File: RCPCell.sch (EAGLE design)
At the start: 22 parts, among them IC1 SIM900, Q1 BSS84, Q2 BSS84, U1 PESDXS4UD

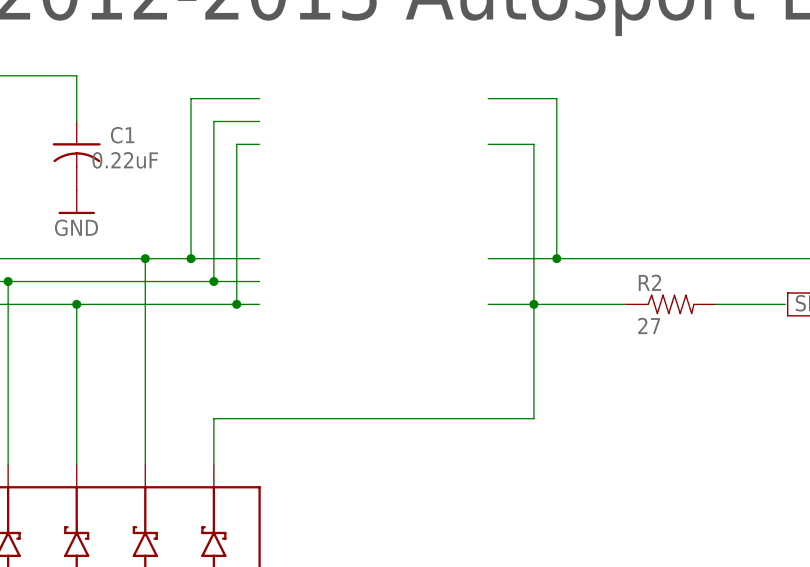
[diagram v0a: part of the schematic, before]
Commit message: placeholder simcard
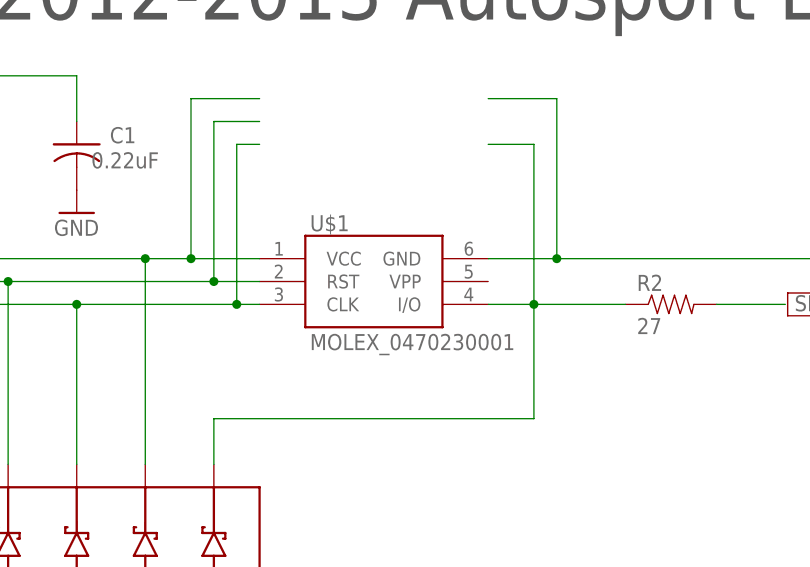
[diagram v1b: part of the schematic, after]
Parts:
- added U$1: MOLEX_0470230001, simcard:MOLEX_0470230001
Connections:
- net GND: now also U$1.GND
- net SIM_CLK_CARD: now also U$1.CLK
- net SIM_DATA_CARD: now also U$1.I/O
- net SIM_RST_CARD: now also U$1.RST
- net SIM_VDD: now also U$1.VCC
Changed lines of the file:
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@@
 <part name="AD156" library="supply2" deviceset="V--&gt;" device="" value=""/>
 <part name="J$1" library="SparkFun" deviceset="SMA_EDGE" device=""/>
+<part name="U$1" library="simcard" deviceset="MOLEX_0470230001" device=""/>
 </parts>
 <sheets>
@@
 </instance>
 <instance part="J$1" gate="1" x="-10.16" y="149.86"/>
+<instance part="U$1" gate="G$1" x="137.16" y="142.24"/>
 </instances>
 <busses>
@@
 <junction x="157.48" y="144.78"/>
 <pinref part="GND7" gate="1" pin="GND"/>
+<pinref part="U$1" gate="G$1" pin="GND"/>
 </segment>
 <segment>
@@
 <pinref part="C1" gate="G$1" pin="1"/>
 <pinref part="U1" gate="G$1" pin="4"/>
+<pinref part="U$1" gate="G$1" pin="VCC"/>
 </segment>
 </net>
@@
 <pinref part="R2" gate="G$1" pin="1"/>
 <pinref part="U1" gate="G$1" pin="6"/>
+<pinref part="U$1" gate="G$1" pin="I/O"/>
 </segment>
 </net>
@@
 <pinref part="R1" gate="G$1" pin="2"/>
 <pinref part="U1" gate="G$1" pin="1"/>
+<pinref part="U$1" gate="G$1" pin="RST"/>
 </segment>
 </net>
@@
 <pinref part="R3" gate="G$1" pin="2"/>
 <pinref part="U1" gate="G$1" pin="3"/>
+<pinref part="U$1" gate="G$1" pin="CLK"/>
 </segment>
 </net>

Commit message: WIP for MK2 version of cell module
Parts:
- U$1: value MOLEX_0470230001 -> MOLEX_04702300012; device simcard:MOLEX_0470230001 -> simcard:MOLEX_04702300012
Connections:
- removed net N$2: NETLIGHT.A, R8.1
- new net N$1: NETLIGHT.C, R8.2
- net GND: now also R8.1; no longer NETLIGHT.C
- net STATUS: now also NETLIGHT.A; no longer R8.2
- net USB_DM_HS_OUT: now also EX1.3; no longer EX1.4
- net USB_DP_HS_OUT: now also EX1.4; no longer EX1.3
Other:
- note added: "Copyright 2012-2014 Autosport Labs"
- note removed: "Copyright 2012-2013 Autosport Labs"
- moved on the sheet: NETLIGHT
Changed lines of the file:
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@@
 <part name="AD156" library="supply2" deviceset="V--&gt;" device="" value=""/>
 <part name="J$1" library="SparkFun" deviceset="SMA_EDGE" device=""/>
-<part name="U$1" library="simcard" deviceset="MOLEX_0470230001" device=""/>
+<part name="U$1" library="simcard" deviceset="MOLEX_0470230001" device="2"/>
 </parts>
 <sheets>
@@
 <plain>
 <text x="109.22" y="-12.7" size="3.81" layer="97" ratio="5">RaceCapture P2P Telemetry</text>
-<text x="200.66" y="177.8" size="6.4516" layer="97" rot="R180">Copyright 2012-2013 Autosport Labs</text>
+<text x="200.66" y="177.8" size="6.4516" layer="97" rot="R180">Copyright 2012-2014 Autosport Labs</text>
 <text x="200.66" y="190.5" size="6.4516" layer="97" rot="R180">RaceCapture Cell Telemetry</text>
 <text x="113.03" y="201.803" size="6.4516" layer="97" font="vector">autosportlabs.com</text>
@@
 <instance part="R8" gate="G$1" x="-187.96" y="-2.54" rot="R90"/>
 <instance part="GND4" gate="1" x="-187.96" y="-22.86"/>
-<instance part="NETLIGHT" gate="G$1" x="-187.96" y="-13.716"/>
+<instance part="NETLIGHT" gate="G$1" x="-187.96" y="9.144"/>
 <instance part="GND62" gate="1" x="104.14" y="7.62"/>
 <instance part="P+16" gate="1" x="175.26" y="63.5"/>
@@
 <nets>
 <net name="GND" class="0">
-<segment>
-<wire x1="-187.96" y1="-17.78" x2="-187.96" y2="-20.32" width="0.1524" layer="91"/>
-<pinref part="GND4" gate="1" pin="GND"/>
-<pinref part="NETLIGHT" gate="G$1" pin="C"/>
-</segment>
 <segment>
 <wire x1="104.14" y1="10.16" x2="104.14" y2="12.7" width="0.1524" layer="91"/>
@@
 </segment>
 <segment>
-<wire x1="149.86" y1="144.78" x2="157.48" y2="144.78" width="0.1524" layer="91"/>
-<wire x1="157.48" y1="144.78" x2="203.2" y2="144.78" width="0.1524" layer="91"/>
+<wire x1="149.86" y1="144.78" x2="203.2" y2="144.78" width="0.1524" layer="91"/>
 <wire x1="203.2" y1="144.78" x2="203.2" y2="134.62" width="0.1524" layer="91"/>
-<wire x1="149.86" y1="162.56" x2="157.48" y2="162.56" width="0.1524" layer="91"/>
-<wire x1="157.48" y1="162.56" x2="157.48" y2="144.78" width="0.1524" layer="91"/>
-<junction x="157.48" y="144.78"/>
 <pinref part="GND7" gate="1" pin="GND"/>
 <pinref part="U$1" gate="G$1" pin="GND"/>
@@
 <junction x="-17.78" y="142.24"/>
 <junction x="-17.78" y="139.7"/>
+</segment>
+<segment>
+<pinref part="R8" gate="G$1" pin="1"/>
+<pinref part="GND4" gate="1" pin="GND"/>
+<wire x1="-187.96" y1="-20.32" x2="-187.96" y2="-7.62" width="0.1524" layer="91"/>
 </segment>
 </net>
@@
 </segment>
 </net>
-<net name="N$2" class="0">
-<segment>
-<wire x1="-187.96" y1="-7.62" x2="-187.96" y2="-10.16" width="0.1524" layer="91"/>
-<pinref part="R8" gate="G$1" pin="1"/>
-<pinref part="NETLIGHT" gate="G$1" pin="A"/>
-</segment>
-</net>
 <net name="+5V" class="0">
 <segment>
@@
 <segment>
 <wire x1="-198.12" y1="17.78" x2="-187.96" y2="17.78" width="0.1524" layer="91"/>
-<wire x1="-187.96" y1="2.54" x2="-187.96" y2="17.78" width="0.1524" layer="91"/>
 <label x="-199.39" y="18.542" size="1.778" layer="95" rot="R180"/>
-<pinref part="R8" gate="G$1" pin="2"/>
+<pinref part="NETLIGHT" gate="G$1" pin="A"/>
+<wire x1="-187.96" y1="17.78" x2="-187.96" y2="12.7" width="0.1524" layer="91"/>
 </segment>
 <segment>
@@
 </segment>
 <segment>
-<wire x1="124.46" y1="144.78" x2="116.84" y2="144.78" width="0.1524" layer="91"/>
-<wire x1="116.84" y1="144.78" x2="111.76" y2="144.78" width="0.1524" layer="91"/>
+<wire x1="124.46" y1="144.78" x2="111.76" y2="144.78" width="0.1524" layer="91"/>
 <wire x1="111.76" y1="144.78" x2="91.44" y2="144.78" width="0.1524" layer="91"/>
 <wire x1="91.44" y1="144.78" x2="91.44" y2="147.32" width="0.1524" layer="91"/>
@@
 <wire x1="104.14" y1="165.1" x2="78.74" y2="165.1" width="0.1524" layer="91"/>
 <wire x1="78.74" y1="165.1" x2="78.74" y2="147.32" width="0.1524" layer="91"/>
-<wire x1="124.46" y1="162.56" x2="116.84" y2="162.56" width="0.1524" layer="91"/>
-<wire x1="116.84" y1="162.56" x2="116.84" y2="144.78" width="0.1524" layer="91"/>
 <wire x1="111.76" y1="121.92" x2="111.76" y2="144.78" width="0.1524" layer="91"/>
 <junction x="78.74" y="147.32"/>
-<junction x="116.84" y="144.78"/>
 <junction x="111.76" y="144.78"/>
 <label x="70.358" y="148.336" size="1.778" layer="95" rot="R180"/>
@@
 <wire x1="154.94" y1="127" x2="119.38" y2="127" width="0.1524" layer="91"/>
 <wire x1="119.38" y1="127" x2="119.38" y2="121.92" width="0.1524" layer="91"/>
-<wire x1="149.86" y1="157.48" x2="154.94" y2="157.48" width="0.1524" layer="91"/>
-<wire x1="154.94" y1="157.48" x2="154.94" y2="139.7" width="0.1524" layer="91"/>
 <junction x="154.94" y="139.7"/>
 <pinref part="R2" gate="G$1" pin="1"/>
@@
 <net name="SIM_RST_CARD" class="0">
 <segment>
-<wire x1="124.46" y1="142.24" x2="119.38" y2="142.24" width="0.1524" layer="91"/>
-<wire x1="119.38" y1="142.24" x2="96.52" y2="142.24" width="0.1524" layer="91"/>
+<wire x1="124.46" y1="142.24" x2="96.52" y2="142.24" width="0.1524" layer="91"/>
 <wire x1="96.52" y1="142.24" x2="93.98" y2="142.24" width="0.1524" layer="91"/>
-<wire x1="124.46" y1="160.02" x2="119.38" y2="160.02" width="0.1524" layer="91"/>
-<wire x1="119.38" y1="160.02" x2="119.38" y2="142.24" width="0.1524" layer="91"/>
 <wire x1="96.52" y1="142.24" x2="96.52" y2="121.92" width="0.1524" layer="91"/>
-<junction x="119.38" y="142.24"/>
 <junction x="96.52" y="142.24"/>
 <pinref part="R1" gate="G$1" pin="2"/>
@@
 <net name="SIM_CLK_CARD" class="0">
 <segment>
-<wire x1="124.46" y1="139.7" x2="121.92" y2="139.7" width="0.1524" layer="91"/>
-<wire x1="121.92" y1="139.7" x2="104.14" y2="139.7" width="0.1524" layer="91"/>
+<wire x1="124.46" y1="139.7" x2="104.14" y2="139.7" width="0.1524" layer="91"/>
 <wire x1="104.14" y1="139.7" x2="91.44" y2="139.7" width="0.1524" layer="91"/>
 <wire x1="91.44" y1="139.7" x2="91.44" y2="137.16" width="0.1524" layer="91"/>
 <wire x1="91.44" y1="137.16" x2="86.36" y2="137.16" width="0.1524" layer="91"/>
-<wire x1="124.46" y1="157.48" x2="121.92" y2="157.48" width="0.1524" layer="91"/>
-<wire x1="121.92" y1="157.48" x2="121.92" y2="139.7" width="0.1524" layer="91"/>
 <wire x1="104.14" y1="121.92" x2="104.14" y2="139.7" width="0.1524" layer="91"/>
-<junction x="121.92" y="139.7"/>
 <junction x="104.14" y="139.7"/>
 <pinref part="R3" gate="G$1" pin="2"/>
@@
 </segment>
 </net>
-<net name="USB_DP_HS_OUT" class="0">
+<net name="USB_DM_HS_OUT" class="0">
 <segment>
 <pinref part="EX1" gate="1" pin="3"/>
@@
 </segment>
 </net>
-<net name="USB_DM_HS_OUT" class="0">
+<net name="USB_DP_HS_OUT" class="0">
 <segment>
 <pinref part="EX1" gate="1" pin="4"/>
@@
 </segment>
 </net>
+<net name="N$1" class="0">
+<segment>
+<pinref part="R8" gate="G$1" pin="2"/>
+<pinref part="NETLIGHT" gate="G$1" pin="C"/>
+<wire x1="-187.96" y1="5.08" x2="-187.96" y2="2.54" width="0.1524" layer="91"/>
+</segment>
+</net>

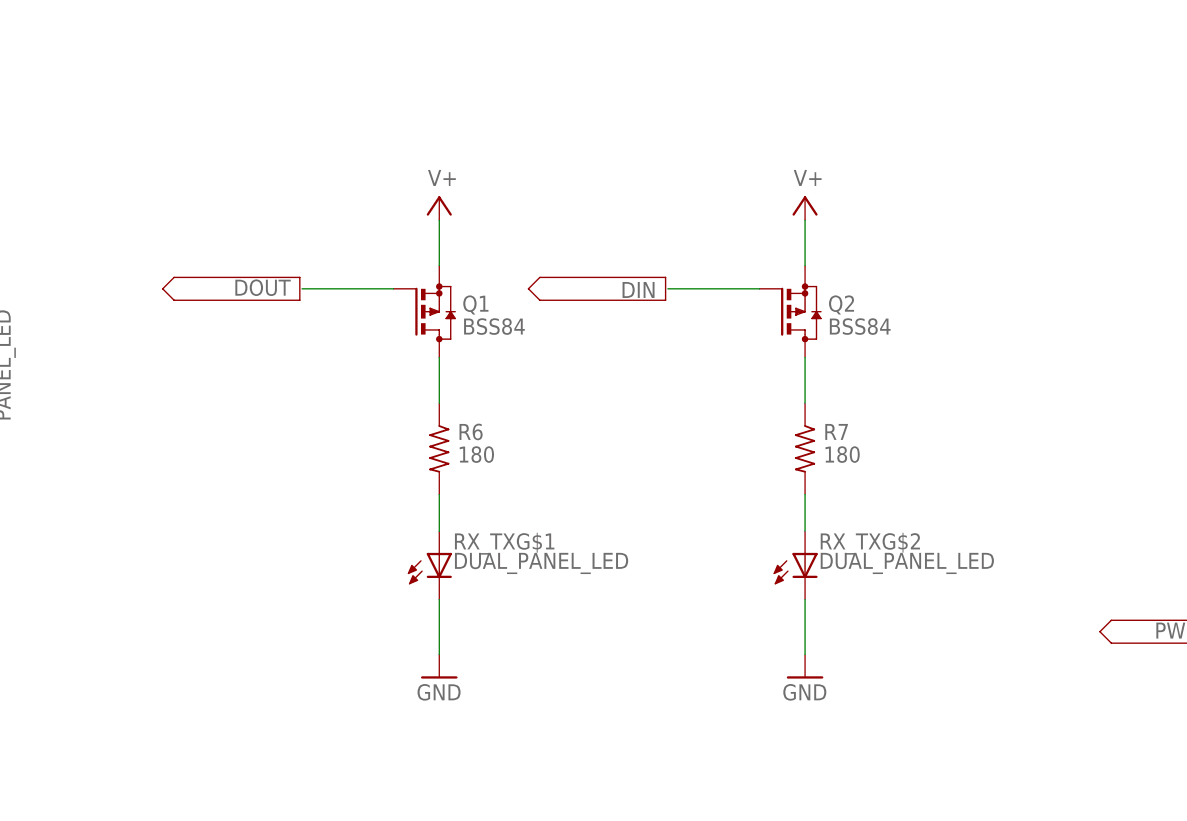
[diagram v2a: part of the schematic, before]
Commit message: WIP for cellular module, compacted board size
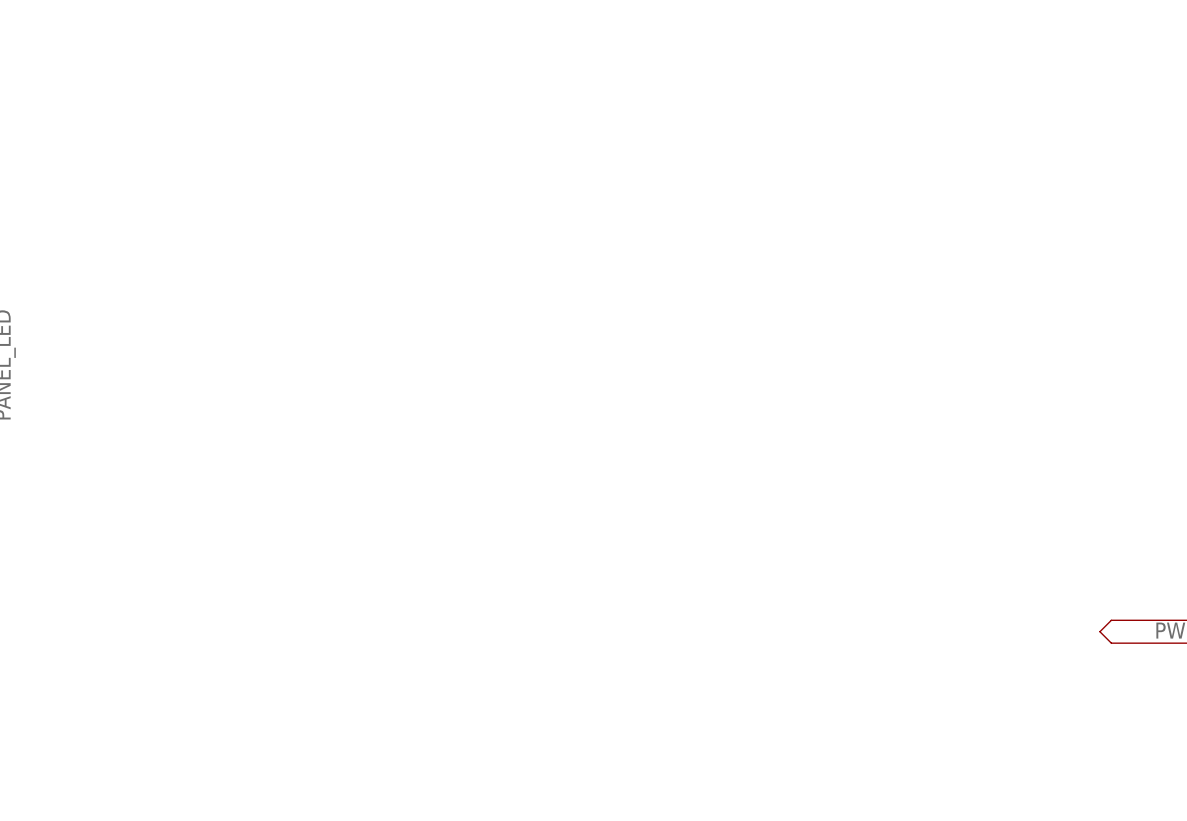
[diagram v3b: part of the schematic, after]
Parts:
- removed Q1, Q2: BSS84, transistor-small-signal:BSS84
- removed R6, R7: 180, rcl:R-US_R0603
- removed RX_TX: DUAL_PANEL_LED, LEDs:DUAL_PANEL_LED
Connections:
- removed net N$3: Q2.D, R7.1
- removed net N$4: R6.2, RX_TXG$1.A
- removed net N$5: Q1.D, R6.1
- removed net N$6: R7.2, RX_TXG$2.A
- net DIN: no longer Q2.G
- net DOUT: no longer Q1.G
- net GND: no longer RX_TXG$1.C, RX_TXG$2.C
- net V+: no longer Q1.S, Q2.S
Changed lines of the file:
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@@
 <part name="C1" library="rcl" deviceset="C-US" device="C0603" value="0.22uF"/>
 <part name="GND9" library="supply1" deviceset="GND" device=""/>
-<part name="R7" library="rcl" deviceset="R-US_" device="R0603" value="180"/>
-<part name="GND31" library="supply1" deviceset="GND" device=""/>
-<part name="RX_TX" library="LEDs" deviceset="DUAL_PANEL_LED" device=""/>
-<part name="P+5" library="supply2" deviceset="V+" device=""/>
-<part name="R6" library="rcl" deviceset="R-US_" device="R0603" value="180"/>
-<part name="GND3" library="supply1" deviceset="GND" device=""/>
-<part name="P+6" library="supply2" deviceset="V+" device=""/>
-<part name="Q1" library="transistor-small-signal" deviceset="BSS84" device=""/>
-<part name="Q2" library="transistor-small-signal" deviceset="BSS84" device=""/>
-<part name="AD9" library="supply2" deviceset="V--&gt;" device="" value=""/>
-<part name="AD11" library="supply2" deviceset="V--&gt;" device="" value=""/>
 <part name="AD10" library="supply2" deviceset="V--&gt;" device="" value=""/>
 <part name="U1" library="smt_diodes" deviceset="PESDXS4UD" device=""/>
@@
 </instance>
 <instance part="GND9" gate="1" x="104.14" y="149.86"/>
-<instance part="R7" gate="G$1" x="-93.98" y="2.54" smashed="yes" rot="R270">
-<attribute name="NAME" x="-91.948" y="3.5306" size="1.778" layer="95"/>
-<attribute name="VALUE" x="-91.948" y="1.016" size="1.778" layer="96"/>
-</instance>
-<instance part="GND31" gate="1" x="-93.98" y="-22.86"/>
-<instance part="RX_TX" gate="G$1" x="-134.62" y="-10.16" smashed="yes">
-<attribute name="NAME" x="-133.096" y="-8.636" size="1.778" layer="95"/>
-<attribute name="VALUE" x="-133.096" y="-10.795" size="1.778" layer="96"/>
-</instance>
-<instance part="RX_TX" gate="G$2" x="-93.98" y="-10.16" smashed="yes">
-<attribute name="NAME" x="-92.456" y="-8.636" size="1.778" layer="95"/>
-<attribute name="VALUE" x="-92.456" y="-10.795" size="1.778" layer="96"/>
-</instance>
-<instance part="P+5" gate="1" x="-93.98" y="30.48"/>
-<instance part="R6" gate="G$1" x="-134.62" y="2.54" smashed="yes" rot="R270">
-<attribute name="NAME" x="-132.588" y="3.5306" size="1.778" layer="95"/>
-<attribute name="VALUE" x="-132.588" y="1.016" size="1.778" layer="96"/>
-</instance>
-<instance part="GND3" gate="1" x="-134.62" y="-22.86"/>
-<instance part="P+6" gate="1" x="-134.62" y="30.48"/>
-<instance part="Q1" gate="G$1" x="-134.62" y="17.78"/>
-<instance part="Q2" gate="G$1" x="-93.98" y="17.78"/>
-<instance part="AD9" gate="G$1" x="-150.114" y="20.32" smashed="yes" rot="R180">
-<attribute name="VALUE" x="-151.384" y="21.082" size="1.778" layer="96" rot="R180"/>
-</instance>
-<instance part="AD11" gate="G$1" x="-109.474" y="20.32" smashed="yes" rot="R180">
-<attribute name="VALUE" x="-110.744" y="21.082" size="1.778" layer="96" rot="R180"/>
-</instance>
 <instance part="AD10" gate="G$1" x="33.02" y="142.494" smashed="yes" rot="R90">
 <attribute name="VALUE" x="33.782" y="143.764" size="1.778" layer="96" rot="R90"/>
@@
 </segment>
 <segment>
-<wire x1="-134.62" y1="-14.224" x2="-134.62" y2="-20.32" width="0.1524" layer="91"/>
-<pinref part="GND3" gate="1" pin="GND"/>
-<pinref part="RX_TX" gate="G$1" pin="C"/>
-</segment>
-<segment>
-<wire x1="-93.98" y1="-14.224" x2="-93.98" y2="-20.32" width="0.1524" layer="91"/>
-<pinref part="GND31" gate="1" pin="GND"/>
-<pinref part="RX_TX" gate="G$2" pin="C"/>
-</segment>
-<segment>
 <wire x1="111.76" y1="99.06" x2="111.76" y2="101.6" width="0.1524" layer="91"/>
 <pinref part="U1" gate="G$1" pin="2"/>
@@
 <pinref part="IC1" gate="G$1" pin="RXD"/>
 </segment>
-<segment>
-<wire x1="-99.06" y1="20.32" x2="-109.22" y2="20.32" width="0.1524" layer="91"/>
-<label x="-110.49" y="21.082" size="1.778" layer="95" rot="R180"/>
-<pinref part="Q2" gate="G$1" pin="G"/>
-</segment>
 </net>
 <net name="DOUT" class="0">
@@
 <label x="-41.402" y="92.202" size="1.778" layer="95" rot="R180"/>
 <pinref part="IC1" gate="G$1" pin="TXD"/>
-</segment>
-<segment>
-<wire x1="-139.7" y1="20.32" x2="-149.86" y2="20.32" width="0.1524" layer="91"/>
-<label x="-151.13" y="21.336" size="1.778" layer="95" rot="R180"/>
-<pinref part="Q1" gate="G$1" pin="G"/>
 </segment>
 </net>
@@
 <pinref part="IC1" gate="VBAT@2" pin="VBAT"/>
 </segment>
-<segment>
-<wire x1="-93.98" y1="27.94" x2="-93.98" y2="22.86" width="0.1524" layer="91"/>
-<pinref part="P+5" gate="1" pin="V+"/>
-<pinref part="Q2" gate="G$1" pin="S"/>
-</segment>
-<segment>
-<wire x1="-134.62" y1="27.94" x2="-134.62" y2="22.86" width="0.1524" layer="91"/>
-<pinref part="P+6" gate="1" pin="V+"/>
-<pinref part="Q1" gate="G$1" pin="S"/>
-</segment>
 </net>
 <net name="+5V" class="0">
@@
 </segment>
 </net>
-<net name="N$3" class="0">
-<segment>
-<wire x1="-93.98" y1="7.62" x2="-93.98" y2="12.7" width="0.1524" layer="91"/>
-<pinref part="R7" gate="G$1" pin="1"/>
-<pinref part="Q2" gate="G$1" pin="D"/>
-</segment>
-</net>
-<net name="N$5" class="0">
-<segment>
-<wire x1="-134.62" y1="7.62" x2="-134.62" y2="12.7" width="0.1524" layer="91"/>
-<pinref part="R6" gate="G$1" pin="1"/>
-<pinref part="Q1" gate="G$1" pin="D"/>
-</segment>
-</net>
-<net name="N$4" class="0">
-<segment>
-<wire x1="-134.62" y1="-6.604" x2="-134.62" y2="-2.54" width="0.1524" layer="91"/>
-<pinref part="R6" gate="G$1" pin="2"/>
-<pinref part="RX_TX" gate="G$1" pin="A"/>
-</segment>
-</net>
-<net name="N$6" class="0">
-<segment>
-<wire x1="-93.98" y1="-6.604" x2="-93.98" y2="-2.54" width="0.1524" layer="91"/>
-<pinref part="R7" gate="G$1" pin="2"/>
-<pinref part="RX_TX" gate="G$2" pin="A"/>
-</segment>
-</net>

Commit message: final layout before incorporating power supply section
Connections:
- net +5V: no longer C11.+
- net SAFE12V: now also C11.+, C12.1
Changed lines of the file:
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@@
 <part name="P+16" library="supply2" deviceset="V+" device=""/>
 <part name="C10" library="rcl" deviceset="CPOL-US" device="SMCD" value="47uF"/>
-<part name="P+27" library="supply1" deviceset="+5V" device=""/>
 <part name="AD70" library="supply2" deviceset="V--&gt;" device="" value=""/>
 <part name="AD72" library="supply2" deviceset="V--&gt;" device="" value=""/>
@@
 <instance part="P+16" gate="1" x="175.26" y="63.5"/>
 <instance part="C10" gate="G$1" x="175.26" y="33.02"/>
-<instance part="P+27" gate="1" x="76.2" y="63.5" smashed="yes">
-<attribute name="VALUE" x="73.66" y="58.42" size="1.778" layer="96" rot="R90"/>
-</instance>
 <instance part="AD70" gate="G$1" x="68.834" y="-12.7" smashed="yes">
 <attribute name="VALUE" x="70.104" y="-13.462" size="1.778" layer="96"/>
@@
 <net name="+5V" class="0">
 <segment>
-<wire x1="76.2" y1="45.72" x2="96.52" y2="45.72" width="0.1524" layer="91"/>
-<wire x1="76.2" y1="45.72" x2="76.2" y2="60.96" width="0.1524" layer="91"/>
-<wire x1="76.2" y1="45.72" x2="76.2" y2="22.86" width="0.1524" layer="91"/>
-<junction x="76.2" y="45.72"/>
-<pinref part="P+27" gate="1" pin="+5V"/>
-<pinref part="C11" gate="G$1" pin="+"/>
-</segment>
-<segment>
 <pinref part="EX2" gate="1" pin="3"/>
 <wire x1="-177.8" y1="104.14" x2="-154.94" y2="104.14" width="0.1524" layer="91"/>
@@
 <wire x1="-170.18" y1="109.22" x2="-170.18" y2="111.76" width="0.1524" layer="91"/>
 </segment>
+<segment>
+<wire x1="76.2" y1="45.72" x2="88.9" y2="45.72" width="0.1524" layer="91"/>
+<wire x1="88.9" y1="45.72" x2="96.52" y2="45.72" width="0.1524" layer="91"/>
+<wire x1="76.2" y1="45.72" x2="76.2" y2="60.96" width="0.1524" layer="91"/>
+<wire x1="76.2" y1="45.72" x2="76.2" y2="22.86" width="0.1524" layer="91"/>
+<junction x="76.2" y="45.72"/>
+<pinref part="C11" gate="G$1" pin="+"/>
+<label x="76.2" y="63.5" size="1.778" layer="95" rot="R90"/>
+<pinref part="C12" gate="G$1" pin="1"/>
+<wire x1="88.9" y1="22.86" x2="88.9" y2="45.72" width="0.1524" layer="91"/>
+<junction x="88.9" y="45.72"/>
+</segment>
 </net>
